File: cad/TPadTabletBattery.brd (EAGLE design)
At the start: 100 x 80 mm, 105 parts, among them J1 MOLEX-MINI-FIT-JR-2POS-RA, J2 USB IN, J3 POWER_JACKPTH, J4 USBA-THRU-UE27-AC54-100, Q1 NCH, Q2 PCH, U1 MCP73833-AMI/UN, U4 PIC24FJ256GB206, U5 MICROCHIP-MINI-DRIVER-MCP1416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

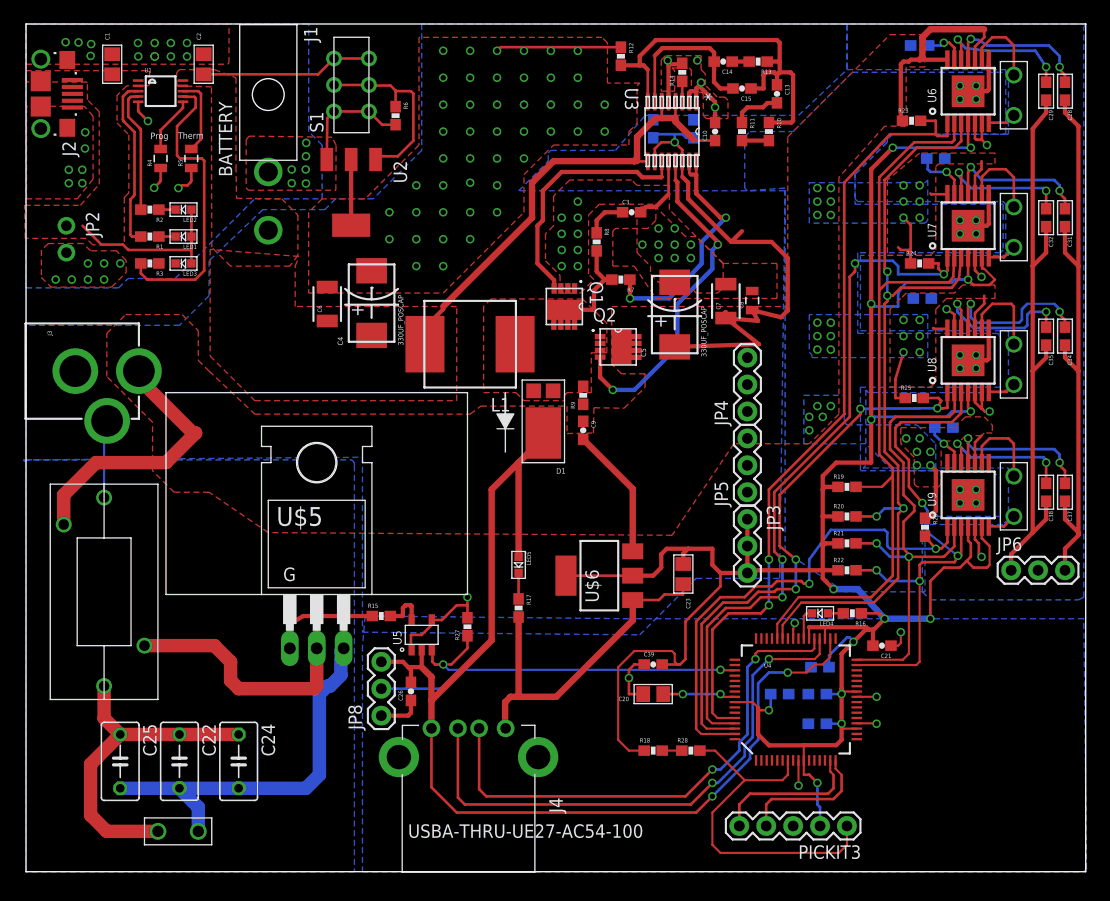
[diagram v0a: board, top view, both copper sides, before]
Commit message: USB OTG board version updated
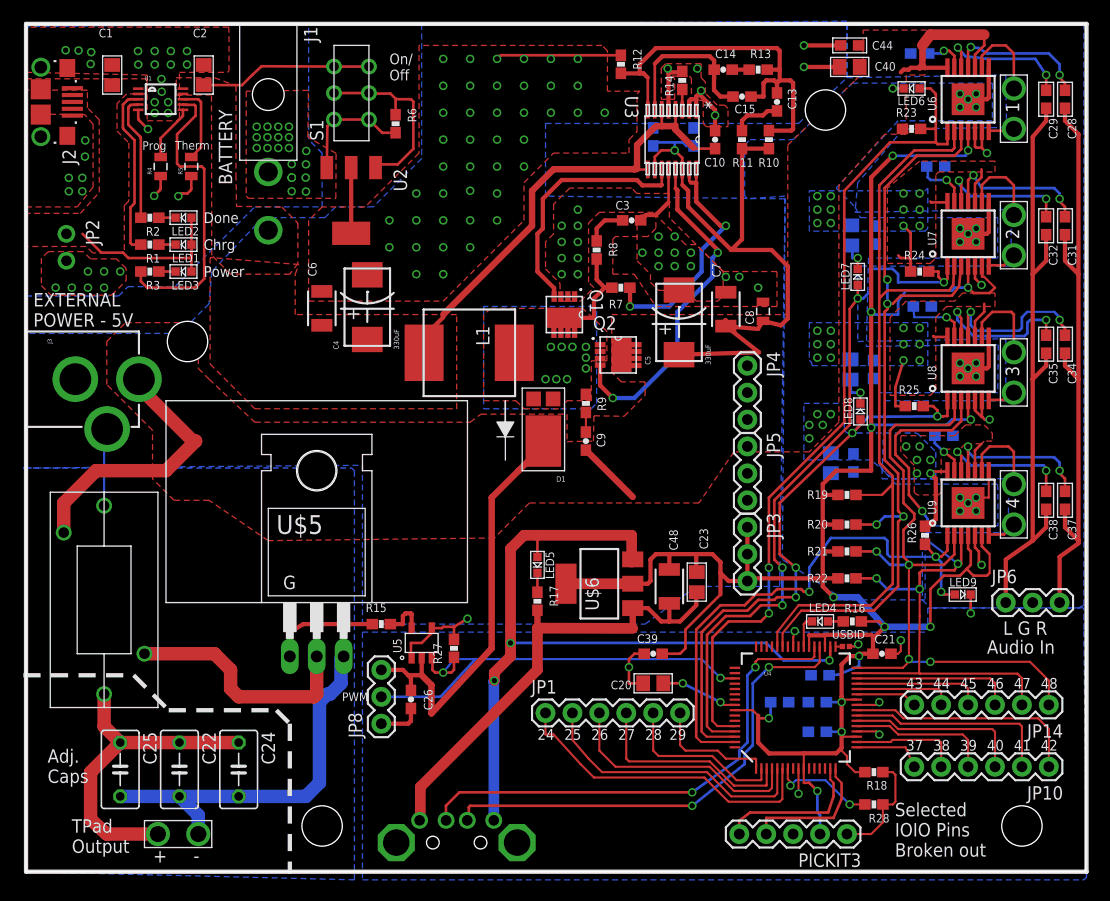
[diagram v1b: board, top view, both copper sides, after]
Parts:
- removed J4: USBA-THRU-UE27-AC54-100, Craig:USBA-THRU
- added C40, C41, C42, C43: 10uF, MCP73833_QFN_v1.0:MICROBUILDER_0805
- added C44, C45, C46, C47: 0.1uF, MCP73833_QFN_v1.0:MICROBUILDER_0603
- added C48: 47uF, SparkFun-Capacitors:1210
- added JP1, JP10, JP14: (no value), SparkFun-Connectors:1X06
- added LED6: F1, MCP73833_QFN_v1.0:MICROBUILDER_CHIPLED_0603
- added LED7: F2, MCP73833_QFN_v1.0:MICROBUILDER_CHIPLED_0603
- added LED8: F3, MCP73833_QFN_v1.0:MICROBUILDER_CHIPLED_0603
- added LED9: F4, MCP73833_QFN_v1.0:MICROBUILDER_CHIPLED_0603
- added U$1: USBA-THRU-PLUG, Craig:USBA-THRU-FLUG
- added U$2: (no value), Craig:TPADTABLETPROJECT
- C28, C29, C31, C32, C34, C35, C37, C38: value 0.1uF -> 0.47uF
- C4, C5: value 330UF_POSCAP -> 330uF
- L1: value (none) -> .82uH
- LED5: value GREEN -> +5V
- moved R18 20.9 mm to (80.0, 9.40)
- moved R28 18.0 mm to (80.0, 6.35), turned to 180 degrees
- moved JP4 4.32 mm to (68.1, 47.8), turned to 270 degrees
- moved JP5 4.32 mm to (68.1, 40.1), turned to 270 degrees
- moved JP6 3.09 mm to (92.5, 25.4)
- moved R27 2.40 mm to (40.4, 21.1)
- moved R17 1.89 mm to (48.3, 25.5)
- moved LED5 1.78 mm to (48.3, 29.0)
- moved C23 1.48 mm to (63.3, 27.3)
- moved C8 1.44 mm to (69.5, 52.9)
- moved JP9 1.27 mm to (93.2, 70.1)
- moved C9 1.05 mm to (52.8, 40.6)
- moved C1 1.02 mm to (8.13, 75.2)
- moved C2 1.02 mm to (16.8, 75.2)
- moved C20 1.02 mm to (59.2, 17.8)
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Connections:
- removed net N$9: R18.2, R28.1
- removed net SCL2: R21.2, U4.32, U8.P$2, U9.P$2
- removed net SDA2: R22.2, U4.31, U8.P$3, U9.P$3
- removed net USBID: U4.33
- new net 5V_USB: LED5.A, U$1.P1, U$6.3, U4.34
- new net N$6: R28.2, U4.7
- new net SCL0: R19.2, U4.44, U6.P$2, U7.P$2
- new net SDA0: R20.2, U4.43, U6.P$3, U7.P$3
- net +3V3: now also C48.1
- net D+: now also U$1.P3; no longer J4.P3
- net D-: now also U$1.P2; no longer J4.P2
- net FAULT1: now also LED6.A
- net FAULT2: now also LED7.A
- net FAULT3: now also LED8.A
- net FAULT4: now also LED9.A
- net GND: now also C40.2, C41.2, C42.2, C43.2, C44.2, C45.2, C46.2, C47.2, C48.2, LED6.C, LED7.C, LED8.C, LED9.C, U$1.P4, U$1.S1, U$1.S2, U4.33; no longer J4.P4, J4.SHD1, J4.SHD2
- net MCLR: now also R18.2, R28.1; no longer R28.2, U4.7
- net PIN24: now also JP1.6
- net PIN25: now also JP1.5
- net PIN26: now also JP1.4
- net PIN27: now also JP1.3
- net PIN28: now also JP1.2
- net PIN29: now also JP1.1
- net PIN37: now also JP10.6
- net PIN38: now also JP10.5
- net PIN39: now also JP10.4
- net PIN40: now also JP10.3
- net PIN41: now also JP10.2
- net PIN42: now also JP10.1
- net PIN43: now also JP14.6
- net PIN44: now also JP14.5
- net PIN45: now also JP14.4
- net PIN46: now also JP14.3
- net SCL1: now also JP14.1, R21.2, U4.32, U8.P$2, U9.P$2; no longer R19.2, U4.44, U6.P$2, U7.P$2
- net SDA1: now also JP14.2, R22.2, U4.31, U8.P$3, U9.P$3; no longer R20.2, U4.43, U6.P$3, U7.P$3
- net VCC: now also C40.1, C41.1, C42.1, C43.1, C44.1, C45.1, C46.1, C47.1; no longer J4.P1, LED5.A, U$6.3, U4.34
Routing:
- net SDA0: track 0.00 -> 77.9 mm, vias 0 -> 4
- net SCL0: track 0.00 -> 75.9 mm
- net 5V_USB: track 0.00 -> 74.9 mm, vias 0 -> 3
- net VCC: track 253.9 -> 185.0 mm, vias 38 -> 36
- net SDA2: track 52.2 -> 0.00 mm, vias 4 -> 0
- net SCL2: track 49.1 -> 0.00 mm, vias 2 -> 0
- net GND: track 171.8 -> 204.4 mm, vias 94 -> 105
- net PIN29: track 0.00 -> 30.1 mm
- net PIN28: track 0.00 -> 26.6 mm
- net PIN27: track 0.00 -> 23.4 mm
- net MCLR: track 33.5 -> 10.7 mm
- net PIN42: track 0.00 -> 22.4 mm
- net PIN26: track 0.00 -> 20.2 mm
- net PIN41: track 0.00 -> 19.8 mm
- net PIN40: track 0.00 -> 16.8 mm
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- added copper zone on layer 16, net SWITCH+
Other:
- board text added: "+"
- board text added: "-"
- board text added: "1"
- board text added: "2"
- board text added: "24"
- board text added: "25"
- board text added: "26"
- board text added: "27"
- board text added: "28"
- board text added: "29"
- board text added: "3"
- board text added: "37"
- board text added: "38"
- board text added: "39"
- board text added: "4"
- board text added: "40"
- board text added: "41"
- board text added: "42"
- board text added: "43"
- board text added: "44"
- board text added: "45"
- board text added: "46"
- board text added: "47"
- board text added: "48"
- board text added: "Adj. Caps"
- board text added: "Audio In"
- board text added: "Chrg"
- board text added: "Done"
- board text added: "EXTERNAL POWER - 5V"
- board text added: "L G R"
- board text added: "On/ Off"
- board text added: "PWM"
- board text added: "Power"
- board text added: "Selected IOIO Pins Broken out"
- board text added: "TPad Output"
- board text added: "USBID"
